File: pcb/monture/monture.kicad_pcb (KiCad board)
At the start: 2 copper layers, 145 x 100 mm, 31 parts, among them U1 Teensy 4.1

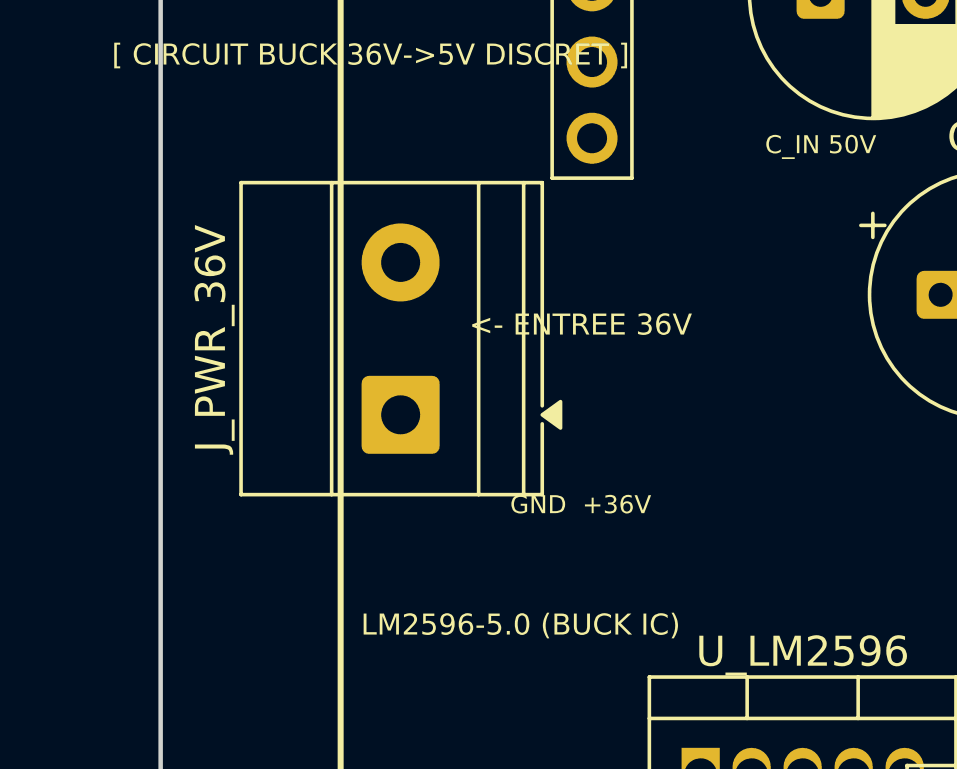
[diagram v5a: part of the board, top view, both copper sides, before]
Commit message: fix(pcb): inversion du sens du bornier 36V pour orienter les ouvertures des fils vers l exterieur gauche
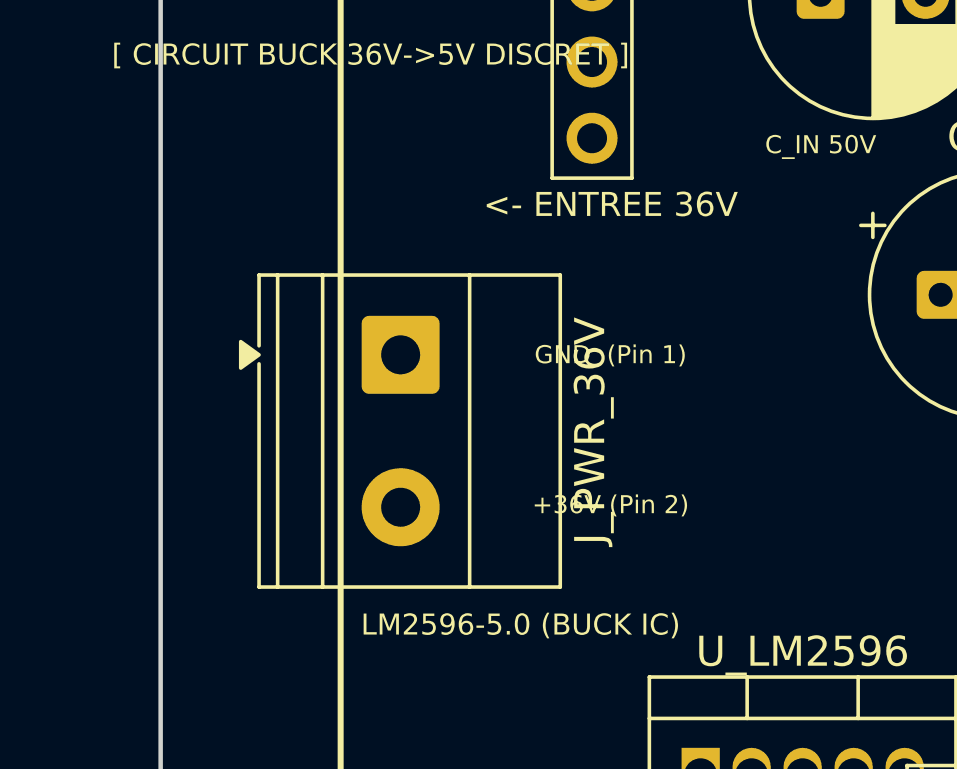
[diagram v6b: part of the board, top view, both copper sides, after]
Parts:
- moved J_PWR_36V 2.00 mm to (8.00, 60.0), turned to -90 degrees
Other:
- board text added: "+36V (Pin 2)"
- board text added: "GND (Pin 1)"
- board text removed: "GND +36V"

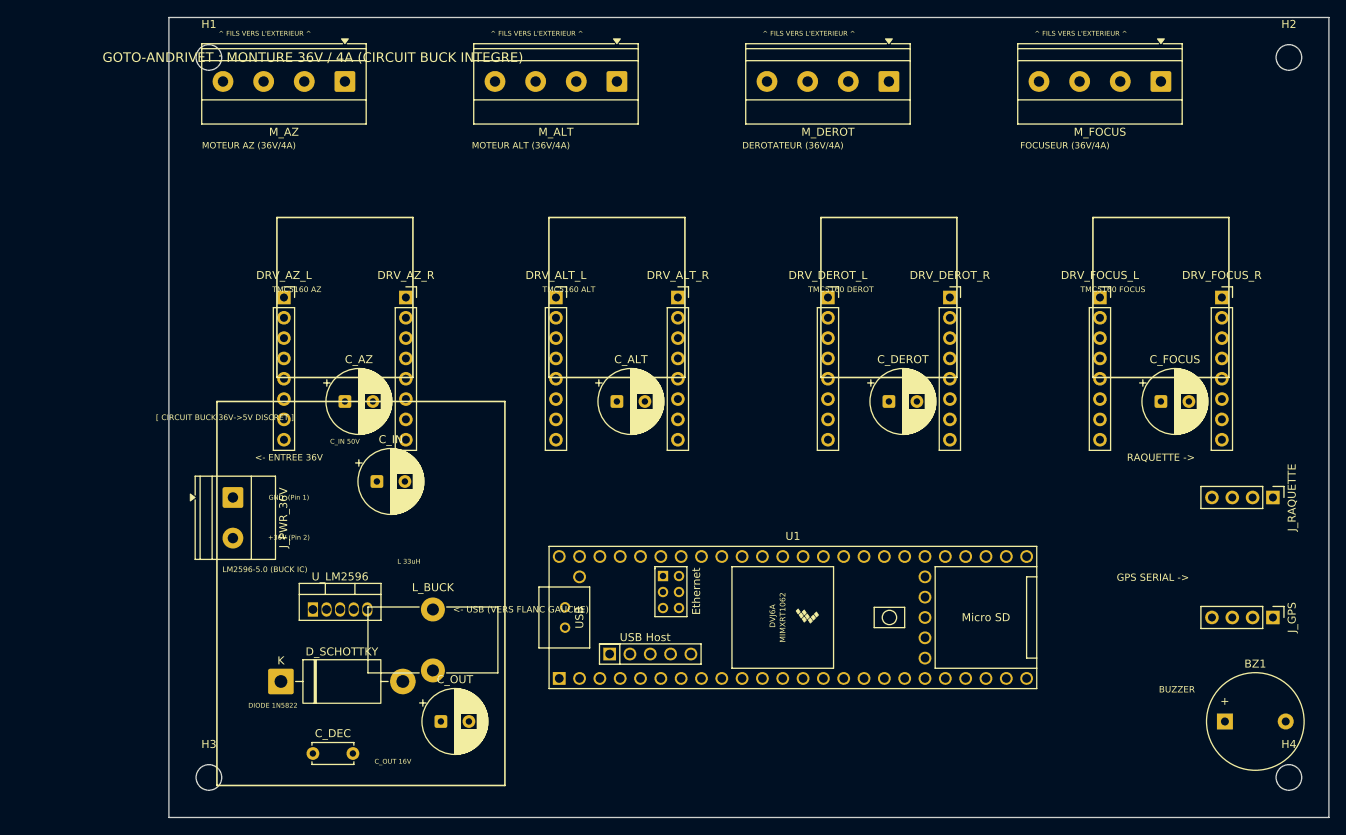
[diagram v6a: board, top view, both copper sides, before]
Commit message: Ajout connecteur USB-A Host sur PCB monture et découpe boîtier 3D
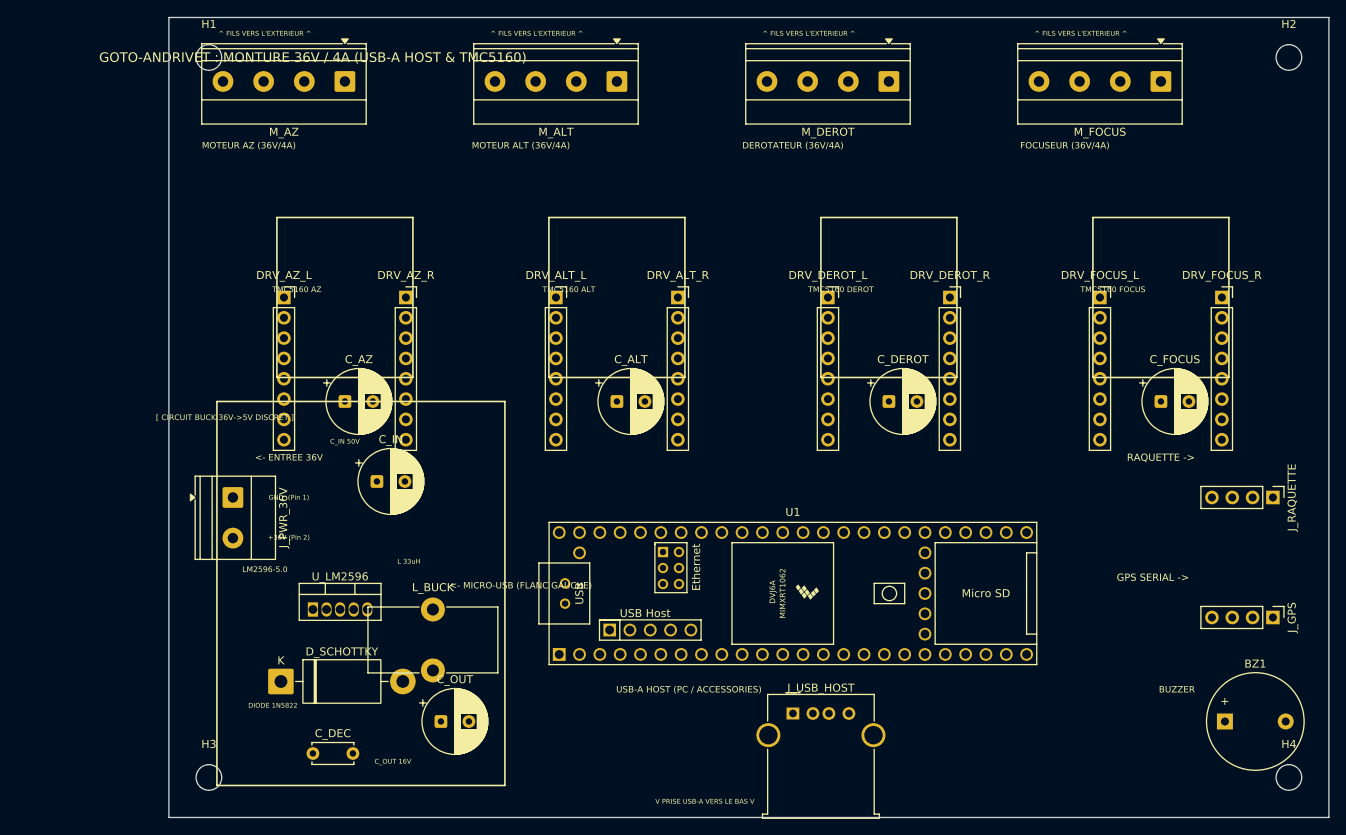
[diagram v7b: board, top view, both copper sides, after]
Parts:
- added J_USB_HOST: USB-A Host, USB_A_Molex_67643_Horizontal, F.Cu at (78.0, 87.0)
- moved U1 3.00 mm to (78.0, 72.0)
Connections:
- U1 pad 55: (no net) -> +5V
- U1 pad 56: (no net) -> USB_HOST_DM
- U1 pad 57: (no net) -> USB_HOST_DP
- U1 pad 58: (no net) -> GND
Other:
- board text added: "<- MICRO-USB (FLANC GAUCHE)"
- board text added: "GOTO-ANDRIVET : MONTURE 36V / 4A (USB-A HOST & TMC5160)"
- board text added: "LM2596-5.0"
- board text added: "USB-A HOST (PC / ACCESSORIES)"
- board text added: "V PRISE USB-A VERS LE BAS V"
- board text removed: "<- USB (VERS FLANC GAUCHE)"
- board text removed: "GOTO-ANDRIVET : MONTURE 36V / 4A (CIRCUIT BUCK INTEGRE)"
- board text removed: "LM2596-5.0 (BUCK IC)"

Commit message: Remplacement du port USB-A par un connecteur USB-B standard pour liaison PC
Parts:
- removed J_USB_HOST: USB-A Host, USB_A_Molex_67643_Horizontal
- added J_USB_PC: USB-B Liaison PC, USB_B_OST_USB-B1HSxx_Horizontal, F.Cu at (79.2, 85.0)
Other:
- board text added: "USB-B (LIAISON PC)"
- board text added: "V PRISE USB-B VERS LE BAS V"
- board text removed: "USB-A HOST (PC / ACCESSORIES)"
- board text removed: "V PRISE USB-A VERS LE BAS V"
